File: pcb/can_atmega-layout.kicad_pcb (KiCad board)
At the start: 2 copper layers, 193 x 96 mm, 300 parts, among them J1 Screw_Terminal_01x02, J2 Screw_Terminal_01x02, J3 Conn_01x04_Female, J4 Connector_female, U1 LM1117-5.0, U2 TJA1051T, U3 MCP2515-xSO, U4 ATmega328P-A, X1 16MHz, X2 16MHz

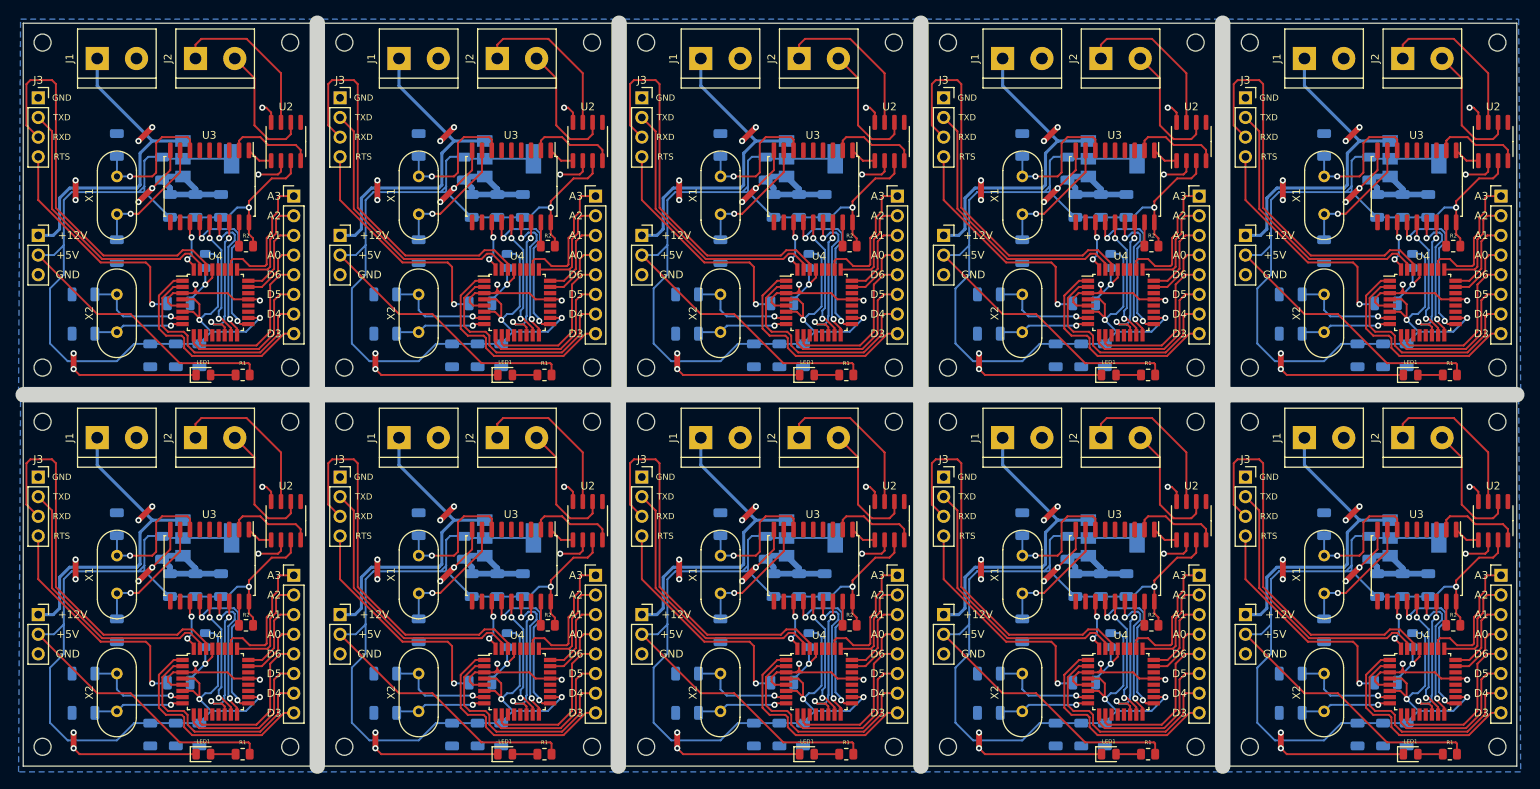
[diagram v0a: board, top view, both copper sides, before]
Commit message: added AVRISP adapter to pcb
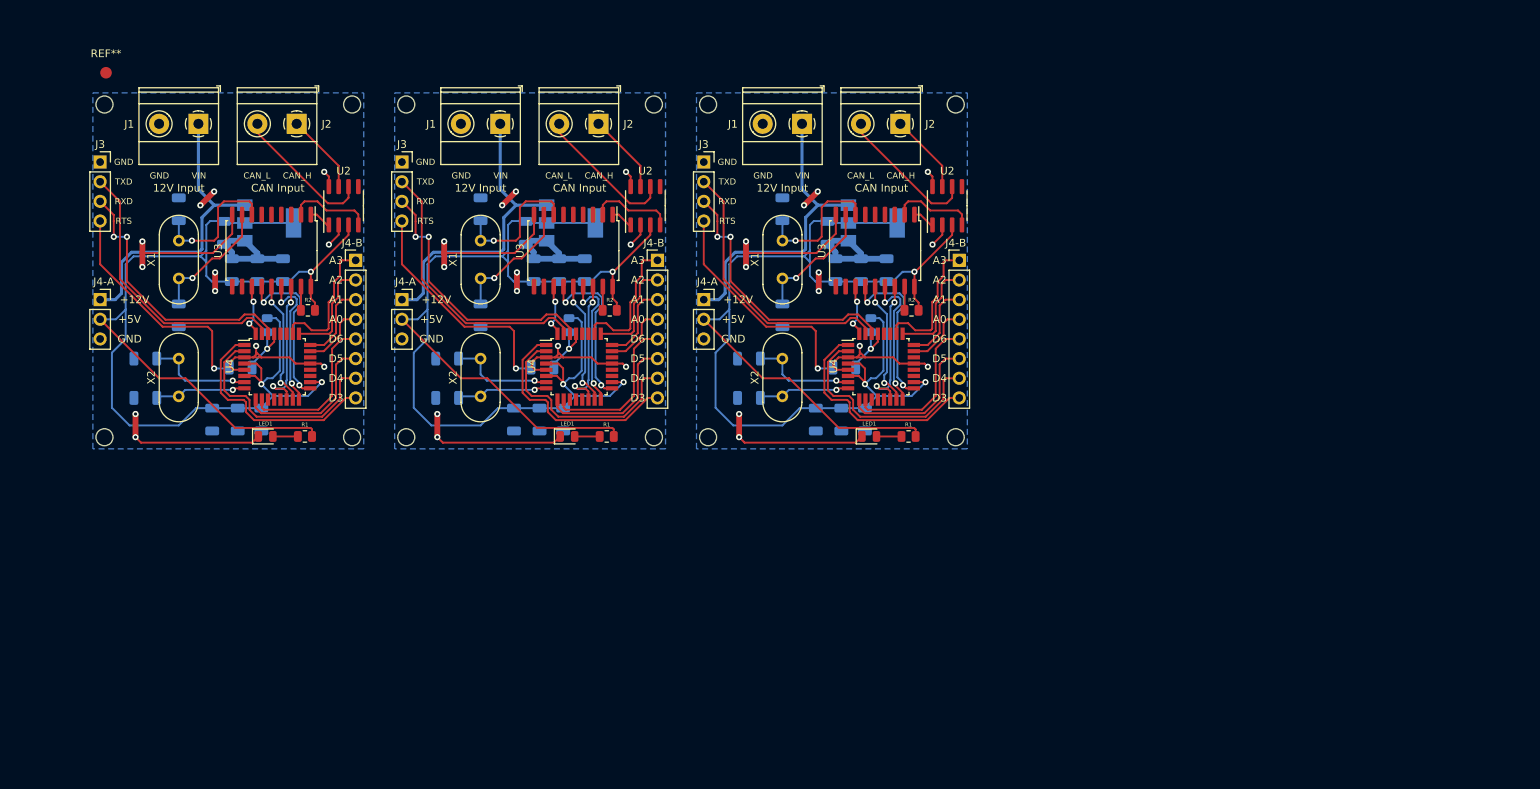
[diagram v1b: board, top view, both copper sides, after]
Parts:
- removed the C1 at (68.9, 79.8)
- removed the C1 at (185.9, 79.8)
- removed the C1 at (29.9, 79.8)
- removed the C1 at (29.9, 30.8)
- removed the C1 at (146.9, 79.8)
- removed the C1 at (185.9, 30.8)
- removed the C1 at (68.9, 30.8)
- removed the C1 at (107.9, 30.8)
- removed the C1 at (107.9, 79.8)
- removed the C1 at (146.9, 30.8)
- removed the C10 at (58.8, 96.0)
- removed the C10 at (136.8, 47.0)
- removed the C10 at (175.8, 96.0)
- removed the C10 at (136.8, 96.0)
- removed the C10 at (19.8, 47.0)
- removed the C10 at (97.8, 96.0)
- removed the C10 at (97.8, 47.0)
- removed the C10 at (175.8, 47.0)
- removed the C10 at (19.8, 96.0)
- removed the C10 at (58.8, 47.0)
- removed the C11 at (19.8, 52.1)
- removed the C11 at (58.8, 101.1)
- removed the C11 at (58.8, 52.1)
- removed the C11 at (97.8, 101.1)
- removed the C11 at (136.8, 101.1)
- removed the C11 at (97.8, 52.1)
- removed the C11 at (19.8, 101.1)
- removed the C11 at (175.8, 52.1)
- removed the C11 at (136.8, 52.1)
- removed the C11 at (175.8, 101.1)
- removed the C12 at (149.1, 97.2)
- removed the C12 at (110.1, 48.2)
- removed the C12 at (188.1, 48.2)
- removed the C12 at (71.1, 48.2)
- removed the C12 at (32.1, 97.2)
- removed the C12 at (32.1, 48.2)
- removed the C12 at (71.1, 97.2)
- removed the C12 at (110.1, 97.2)
- removed the C12 at (149.1, 48.2)
- removed the C12 at (188.1, 97.2)
- removed the C2 at (109.0, 84.6)
- removed the C2 at (148.0, 84.6)
- removed the C2 at (187.0, 84.6)
- removed the C2 at (31.0, 84.6)
- removed the C2 at (70.0, 84.6)
- removed the C2 at (109.0, 35.6)
- removed the C2 at (187.0, 35.6)
- removed the C2 at (70.0, 35.6)
- removed the C2 at (148.0, 35.6)
- removed the C2 at (31.0, 35.6)
- removed the C3 at (34.3, 84.6)
- removed the C3 at (34.3, 35.6)
- removed the C3 at (73.3, 84.6)
- removed the C3 at (73.3, 35.6)
- removed the C3 at (190.3, 35.6)
- removed the C3 at (190.3, 84.6)
- removed the C3 at (112.3, 84.6)
- removed the C3 at (112.3, 35.6)
- removed the C3 at (151.3, 84.6)
- removed the C3 at (151.3, 35.6)
- removed the C4 at (115.6, 35.6)
- removed the C4 at (76.6, 84.6)
- removed the C4 at (193.6, 84.6)
- removed the C4 at (37.6, 84.6)
- removed the C4 at (154.6, 84.6)
- removed the C4 at (37.6, 35.6)
- removed the C4 at (154.6, 35.6)
- removed the C4 at (76.6, 35.6)
- removed the C4 at (193.6, 35.6)
- removed the C4 at (115.6, 84.6)
- removed the C5 at (63.1, 90.5)
- removed the C5 at (63.1, 41.5)
- removed the C5 at (141.1, 90.5)
- removed the C5 at (102.1, 41.5)
- removed the C5 at (24.1, 90.5)
- removed the C5 at (180.1, 41.5)
- removed the C5 at (180.1, 90.5)
- removed the C5 at (141.1, 41.5)
- removed the C5 at (102.1, 90.5)
- removed the C5 at (24.1, 41.5)
- removed the C6 at (180.1, 76.7)
- removed the C6 at (141.1, 76.7)
- removed the C6 at (102.1, 27.7)
- removed the C6 at (63.1, 27.7)
- removed the C6 at (24.1, 27.7)
- removed the C6 at (180.1, 27.7)
- removed the C6 at (63.1, 76.7)
- removed the C6 at (141.1, 27.7)
- removed the C6 at (102.1, 76.7)
- removed the C6 at (24.1, 76.7)
- removed the C7 at (31.7, 54.9)
- removed the C7 at (187.7, 103.9)
- removed the C7 at (187.7, 54.9)
- removed the C7 at (148.7, 54.9)
- removed the C7 at (31.7, 103.9)
- removed the C7 at (70.7, 54.9)
- removed the C7 at (109.7, 54.9)
- removed the C7 at (70.7, 103.9)
- removed the C7 at (148.7, 103.9)
- removed the C7 at (109.7, 103.9)
- removed the C8 at (112.8, 54.9)
- removed the C8 at (73.8, 103.9)
- removed the C8 at (151.8, 54.9)
- removed the C8 at (112.8, 103.9)
- removed the C8 at (34.8, 103.9)
- removed the C8 at (34.8, 54.9)
- removed the C8 at (73.8, 54.9)
- removed the C8 at (190.8, 54.9)
- removed the C8 at (190.8, 103.9)
- removed the C8 at (151.8, 103.9)
- removed the C9 at (145.4, 54.9)
- removed the C9 at (67.4, 103.9)
- removed the C9 at (145.4, 103.9)
- removed the C9 at (184.4, 103.9)
- removed the C9 at (28.4, 54.9)
- removed the C9 at (67.4, 54.9)
- removed the C9 at (28.4, 103.9)
- removed the C9 at (106.4, 103.9)
- removed the C9 at (106.4, 54.9)
- removed the C9 at (184.4, 54.9)
- removed the J1 at (21.6, 16.6)
- removed the J1 at (99.6, 16.6)
- removed the J1 at (60.6, 16.6)
- removed the J1 at (138.6, 16.6)
- removed the J1 at (99.6, 65.6)
- removed the J1 at (21.6, 65.6)
- removed the J1 at (60.6, 65.6)
- removed the J1 at (138.6, 65.6)
- removed the J1 at (177.6, 16.6)
- removed the J1 at (177.6, 65.6)
- removed the J2 at (112.3, 16.6)
- removed the J2 at (151.3, 65.6)
- removed the J2 at (112.3, 65.6)
- removed the J2 at (190.3, 65.6)
- removed the J2 at (151.3, 16.6)
- removed the J2 at (190.3, 16.6)
- removed the J2 at (34.3, 65.6)
- removed the J2 at (73.3, 65.6)
- removed the J2 at (73.3, 16.6)
- removed the J2 at (34.3, 16.6)
- removed the J3 at (13.9, 70.6)
- removed the J3 at (169.9, 70.6)
- removed the J3 at (130.9, 70.6)
- removed the J3 at (169.9, 21.6)
- removed the J3 at (91.9, 21.6)
- removed the J3 at (91.9, 70.6)
- removed the J3 at (52.9, 21.6)
- removed the J3 at (52.9, 70.6)
- removed the J3 at (13.9, 21.6)
- removed the J3 at (130.9, 21.6)
- removed J4 (x10): Connector_female, CAN_ATmega:Connector_female
- removed the LED1 at (113.3, 106.5)
- removed the LED1 at (74.3, 106.5)
- removed the LED1 at (35.3, 57.5)
- removed the LED1 at (152.3, 106.5)
- removed the LED1 at (113.3, 57.5)
- removed the LED1 at (74.3, 57.5)
- removed the LED1 at (152.3, 57.5)
- removed the LED1 at (191.3, 106.5)
- removed the LED1 at (35.3, 106.5)
- removed the LED1 at (191.3, 57.5)
- removed the R1 at (40.4, 57.5)
- removed the R1 at (118.4, 57.5)
- removed the R1 at (157.4, 106.5)
- removed the R1 at (196.4, 106.5)
- removed the R1 at (40.4, 106.5)
- removed the R1 at (196.4, 57.5)
- removed the R1 at (79.4, 106.5)
- removed the R1 at (157.4, 57.5)
- removed the R1 at (118.4, 106.5)
- removed the R1 at (79.4, 57.5)
- removed the R2 at (40.8, 89.8)
- removed the R2 at (157.8, 89.8)
- removed the R2 at (196.8, 89.8)
- removed the R2 at (196.8, 40.8)
- removed the R2 at (157.8, 40.8)
- removed the R2 at (79.8, 40.8)
- removed the R2 at (118.8, 89.8)
- removed the R2 at (79.8, 89.8)
- removed the R2 at (118.8, 40.8)
- removed the R2 at (40.8, 40.8)
- removed the R3 at (152.5, 91.7)
- removed the R3 at (74.5, 91.7)
- removed the R3 at (35.5, 42.7)
- removed the R3 at (113.5, 91.7)
- removed the R3 at (191.5, 91.7)
- removed the R3 at (113.5, 42.7)
- removed the R3 at (74.5, 42.7)
- removed the R3 at (152.5, 42.7)
- removed the R3 at (35.5, 91.7)
- removed the R3 at (191.5, 42.7)
- removed the REF** at (53.5, 14.5)
- removed the REF** at (92.5, 14.5)
- removed the REF** at (14.5, 63.5)
- removed the REF** at (170.5, 56.5)
- removed the REF** at (124.5, 14.5)
- removed the REF** at (85.5, 63.5)
- removed the REF** at (85.5, 14.5)
- removed the REF** at (124.5, 63.5)
- removed the REF** at (53.5, 56.5)
- removed the REF** at (92.5, 63.5)
- removed the REF** at (170.5, 14.5)
- removed the REF** at (14.5, 14.5)
- removed the REF** at (131.5, 14.5)
- removed the REF** at (131.5, 56.5)
- removed the REF** at (14.5, 56.5)
- removed the REF** at (124.5, 105.5)
- removed the REF** at (170.5, 105.5)
- removed the REF** at (14.5, 105.5)
- removed the REF** at (163.5, 63.5)
- removed the REF** at (163.5, 105.5)
- removed the REF** at (53.5, 63.5)
- removed the REF** at (202.5, 14.5)
- removed the REF** at (46.5, 56.5)
- removed the REF** at (53.5, 105.5)
- removed the REF** at (46.5, 14.5)
- removed the REF** at (202.5, 105.5)
- removed the REF** at (131.5, 105.5)
- removed the REF** at (85.5, 56.5)
- removed the REF** at (163.5, 56.5)
- removed the REF** at (124.5, 56.5)
- removed the REF** at (46.5, 105.5)
- removed the REF** at (92.5, 56.5)
- removed the REF** at (163.5, 14.5)
- removed the REF** at (202.5, 56.5)
- removed the REF** at (131.5, 63.5)
- removed the REF** at (85.5, 105.5)
- removed the REF** at (46.5, 63.5)
- removed the REF** at (202.5, 63.5)
- removed the REF** at (170.5, 63.5)
- removed the REF** at (92.5, 105.5)
- removed the U1 at (191.8, 78.5)
- removed the U1 at (152.8, 78.5)
- removed the U1 at (152.8, 29.5)
- removed the U1 at (35.8, 78.5)
- removed the U1 at (35.8, 29.5)
- removed the U1 at (191.8, 29.5)
- removed the U1 at (74.8, 78.5)
- removed the U1 at (113.8, 78.5)
- removed the U1 at (113.8, 29.5)
- removed the U1 at (74.8, 29.5)
- removed the U2 at (84.9, 27.3)
- removed the U2 at (201.9, 27.3)
- removed the U2 at (84.9, 76.3)
- removed the U2 at (45.9, 76.3)
- removed the U2 at (123.9, 76.3)
- removed the U2 at (162.9, 27.3)
- removed the U2 at (201.9, 76.3)
- removed the U2 at (162.9, 76.3)
- removed the U2 at (123.9, 27.3)
- removed the U2 at (45.9, 27.3)
- removed the U3 at (75.1, 33.1)
- removed the U3 at (153.1, 82.1)
- removed the U3 at (192.1, 82.1)
- removed the U3 at (36.1, 82.1)
- removed the U3 at (75.1, 82.1)
- removed the U3 at (153.1, 33.1)
- removed the U3 at (192.1, 33.1)
- removed the U3 at (36.1, 33.1)
- removed the U3 at (114.1, 82.1)
- removed the U3 at (114.1, 33.1)
- removed the U4 at (75.8, 48.1)
- removed the U4 at (153.8, 48.1)
- removed the U4 at (114.8, 48.1)
- removed the U4 at (114.8, 97.1)
- removed the U4 at (36.8, 48.1)
- removed the U4 at (192.8, 48.1)
- removed the U4 at (75.8, 97.1)
- removed the U4 at (36.8, 97.1)
- removed the U4 at (153.8, 97.1)
- removed the U4 at (192.8, 97.1)
- removed the X1 at (63.1, 80.8)
- removed the X1 at (24.1, 80.8)
- removed the X1 at (141.1, 80.8)
- removed the X1 at (180.1, 80.8)
- removed the X1 at (180.1, 31.8)
- removed the X1 at (102.1, 80.8)
- removed the X1 at (141.1, 31.8)
- removed the X1 at (63.1, 31.8)
- removed the X1 at (24.1, 31.8)
- removed the X1 at (102.1, 31.8)
- removed the X2 at (102.1, 96.0)
- removed the X2 at (63.1, 96.0)
- removed the X2 at (102.1, 47.0)
- removed the X2 at (24.1, 96.0)
- removed the X2 at (180.1, 96.0)
- removed the X2 at (63.1, 47.0)
- removed the X2 at (141.1, 96.0)
- removed the X2 at (24.1, 47.0)
- removed the X2 at (180.1, 47.0)
- removed the X2 at (141.1, 47.0)
- added C1: 1uF, Capacitor_SMD:C_1206_3216Metric, B.Cu at (37.9, 39.1)
- added C1: 1uF, Capacitor_SMD:C_1206_3216Metric, B.Cu at (76.9, 39.1)
- added C1: 1uF, Capacitor_SMD:C_1206_3216Metric, B.Cu at (115.9, 39.1)
- added C10: 22PF, Capacitor_SMD:C_1206_3216Metric, B.Cu at (66.8, 55.3)
- added C10: 22PF, Capacitor_SMD:C_1206_3216Metric, B.Cu at (27.8, 55.3)
- added C10: 22PF, Capacitor_SMD:C_1206_3216Metric, B.Cu at (105.8, 55.3)
- added C11: 22PF, Capacitor_SMD:C_1206_3216Metric, B.Cu at (105.8, 60.4)
- added C11: 22PF, Capacitor_SMD:C_1206_3216Metric, B.Cu at (27.8, 60.4)
- added C11: 22PF, Capacitor_SMD:C_1206_3216Metric, B.Cu at (66.8, 60.4)
- added C12: 1uF, Capacitor_SMD:C_1206_3216Metric, B.Cu at (79.1, 56.5)
- added C12: 1uF, Capacitor_SMD:C_1206_3216Metric, B.Cu at (118.1, 56.5)
- added C12: 1uF, Capacitor_SMD:C_1206_3216Metric, B.Cu at (40.1, 56.5)
- added C2: 10uF/16V, Capacitor_SMD:C_1206_3216Metric, B.Cu at (117.0, 43.9)
- added C2: 10uF/16V, Capacitor_SMD:C_1206_3216Metric, B.Cu at (39.0, 43.9)
- added C2: 10uF/16V, Capacitor_SMD:C_1206_3216Metric, B.Cu at (78.0, 43.9)
- added C3: 0.1uF, Capacitor_SMD:C_1206_3216Metric, B.Cu at (81.3, 43.9)
- added C3: 0.1uF, Capacitor_SMD:C_1206_3216Metric, B.Cu at (42.3, 43.9)
- added C3: 0.1uF, Capacitor_SMD:C_1206_3216Metric, B.Cu at (120.3, 43.9)
- added C4: 0.1uF, Capacitor_SMD:C_1206_3216Metric, B.Cu at (123.6, 43.9)
- added C4: 0.1uF, Capacitor_SMD:C_1206_3216Metric, B.Cu at (45.6, 43.9)
- added C4: 0.1uF, Capacitor_SMD:C_1206_3216Metric, B.Cu at (84.6, 43.9)
- added C5: 22PF, Capacitor_SMD:C_1206_3216Metric, B.Cu at (71.1, 49.8)
- added C5: 22PF, Capacitor_SMD:C_1206_3216Metric, B.Cu at (32.1, 49.8)
- added C5: 22PF, Capacitor_SMD:C_1206_3216Metric, B.Cu at (110.1, 49.8)
- added C6: 22PF, Capacitor_SMD:C_1206_3216Metric, B.Cu at (110.1, 36.0)
- added C6: 22PF, Capacitor_SMD:C_1206_3216Metric, B.Cu at (71.1, 36.0)
- added C6: 22PF, Capacitor_SMD:C_1206_3216Metric, B.Cu at (32.1, 36.0)
- added C7: 0.1uF, Capacitor_SMD:C_1206_3216Metric, B.Cu at (78.7, 63.2)
- added C7: 0.1uF, Capacitor_SMD:C_1206_3216Metric, B.Cu at (39.7, 63.2)
- added C7: 0.1uF, Capacitor_SMD:C_1206_3216Metric, B.Cu at (117.7, 63.2)
- added C8: 10uF/16V, Capacitor_SMD:C_1206_3216Metric, B.Cu at (120.8, 63.2)
- added C8: 10uF/16V, Capacitor_SMD:C_1206_3216Metric, B.Cu at (42.8, 63.2)
- added C8: 10uF/16V, Capacitor_SMD:C_1206_3216Metric, B.Cu at (81.8, 63.2)
- added C9: 0.1uF, Capacitor_SMD:C_1206_3216Metric, B.Cu at (114.4, 63.2)
- added C9: 0.1uF, Capacitor_SMD:C_1206_3216Metric, B.Cu at (75.4, 63.2)
- added C9: 0.1uF, Capacitor_SMD:C_1206_3216Metric, B.Cu at (36.4, 63.2)
- added J1: Screw_Terminal_01x02, TerminalBlock_Phoenix:TerminalBlock_Phoenix_MKDS-1,5-2-5.08_1x02_P5.08mm_Horizontal, F.Cu at (73.6, 25.0)
- added J1: Screw_Terminal_01x02, TerminalBlock_Phoenix:TerminalBlock_Phoenix_MKDS-1,5-2-5.08_1x02_P5.08mm_Horizontal, F.Cu at (34.6, 25.0)
- added J1: Screw_Terminal_01x02, TerminalBlock_Phoenix:TerminalBlock_Phoenix_MKDS-1,5-2-5.08_1x02_P5.08mm_Horizontal, F.Cu at (112.6, 25.0)
- added J2: Screw_Terminal_01x02, TerminalBlock_Phoenix:TerminalBlock_Phoenix_MKDS-1,5-2-5.08_1x02_P5.08mm_Horizontal, F.Cu at (86.3, 25.0)
- added J2: Screw_Terminal_01x02, TerminalBlock_Phoenix:TerminalBlock_Phoenix_MKDS-1,5-2-5.08_1x02_P5.08mm_Horizontal, F.Cu at (125.3, 25.0)
- added J2: Screw_Terminal_01x02, TerminalBlock_Phoenix:TerminalBlock_Phoenix_MKDS-1,5-2-5.08_1x02_P5.08mm_Horizontal, F.Cu at (47.3, 25.0)
- added J3: Conn_01x04_Female, Connector_PinSocket_2.54mm:PinSocket_1x04_P2.54mm_Vertical, F.Cu at (60.9, 29.9)
- added J3: Conn_01x04_Female, Connector_PinSocket_2.54mm:PinSocket_1x04_P2.54mm_Vertical, F.Cu at (99.9, 29.9)
- added J3: Conn_01x04_Female, Connector_PinSocket_2.54mm:PinSocket_1x04_P2.54mm_Vertical, F.Cu at (21.9, 29.9)
- added J4-A: Connector_female, CAN_ATmega:Connector_female, F.Cu at (37.2, 50.3)
- added J4-A: Connector_female, CAN_ATmega:Connector_female, F.Cu at (115.2, 50.3)
- added J4-A: Connector_female, CAN_ATmega:Connector_female, F.Cu at (76.2, 50.3)
- added LED1: Green, LED_SMD:LED_0805_2012Metric, F.Cu at (82.3, 65.4)
- added LED1: Green, LED_SMD:LED_0805_2012Metric, F.Cu at (121.3, 65.4)
- added LED1: Green, LED_SMD:LED_0805_2012Metric, F.Cu at (43.3, 65.4)
- added R1: 1K, Resistor_SMD:R_0805_2012Metric, F.Cu at (48.4, 65.4)
- added R1: 1K, Resistor_SMD:R_0805_2012Metric, F.Cu at (87.4, 65.4)
- added R1: 1K, Resistor_SMD:R_0805_2012Metric, F.Cu at (126.4, 65.4)
- added R2: 10K, Resistor_SMD:R_0805_2012Metric, F.Cu at (48.8, 49.1)
- added R2: 10K, Resistor_SMD:R_0805_2012Metric, F.Cu at (126.8, 49.1)
- added R2: 10K, Resistor_SMD:R_0805_2012Metric, F.Cu at (87.8, 49.1)
- added R3: 10K, Resistor_SMD:R_0805_2012Metric, B.Cu at (43.5, 51.0)
- added R3: 10K, Resistor_SMD:R_0805_2012Metric, B.Cu at (82.5, 51.0)
- added R3: 10K, Resistor_SMD:R_0805_2012Metric, B.Cu at (121.5, 51.0)
- added REF**: MountingHole_2.2mm_M2, MountingHole:MountingHole_2.2mm_M2, F.Cu at (61.5, 22.5)
- added REF**: MountingHole_2.2mm_M2, MountingHole:MountingHole_2.2mm_M2, F.Cu at (22.5, 65.5)
- added REF**: MountingHole_2.2mm_M2, MountingHole:MountingHole_2.2mm_M2, F.Cu at (54.5, 65.5)
- added REF**: MountingHole_2.2mm_M2, MountingHole:MountingHole_2.2mm_M2, F.Cu at (100.5, 22.5)
- added REF**: MountingHole_2.2mm_M2, MountingHole:MountingHole_2.2mm_M2, F.Cu at (54.5, 22.5)
- added REF**: MountingHole_2.2mm_M2, MountingHole:MountingHole_2.2mm_M2, F.Cu at (93.5, 22.5)
- added REF**: MountingHole_2.2mm_M2, MountingHole:MountingHole_2.2mm_M2, F.Cu at (22.5, 22.5)
- added REF**: MountingHole_2.2mm_M2, MountingHole:MountingHole_2.2mm_M2, F.Cu at (93.5, 65.5)
- added REF**: MountingHole_2.2mm_M2, MountingHole:MountingHole_2.2mm_M2, F.Cu at (132.5, 65.5)
- added REF**: Fiducial_1.5mm_Mask3mm, Fiducial:Fiducial_1.5mm_Mask3mm, F.Cu at (22.7, 18.4)
- added REF**: MountingHole_2.2mm_M2, MountingHole:MountingHole_2.2mm_M2, F.Cu at (132.5, 22.5)
- added REF**: MountingHole_2.2mm_M2, MountingHole:MountingHole_2.2mm_M2, F.Cu at (100.5, 65.5)
- added REF**: MountingHole_2.2mm_M2, MountingHole:MountingHole_2.2mm_M2, F.Cu at (61.5, 65.5)
- added U1: LM1117-5.0, Package_TO_SOT_SMD:SOT-223, B.Cu at (82.8, 37.8)
- added U1: LM1117-5.0, Package_TO_SOT_SMD:SOT-223, B.Cu at (43.8, 37.8)
- added U1: LM1117-5.0, Package_TO_SOT_SMD:SOT-223, B.Cu at (121.8, 37.8)
- added U2: TJA1051T, Package_SO:SOIC-8_3.9x4.9mm_P1.27mm, F.Cu at (53.4, 35.6)
- added U2: TJA1051T, Package_SO:SOIC-8_3.9x4.9mm_P1.27mm, F.Cu at (92.4, 35.6)
- added U2: TJA1051T, Package_SO:SOIC-8_3.9x4.9mm_P1.27mm, F.Cu at (131.4, 35.6)
- added U3: MCP2515-xSO, Package_SO:SOIC-18W_7.5x11.6mm_P1.27mm, F.Cu at (83.1, 41.4)
- added U3: MCP2515-xSO, Package_SO:SOIC-18W_7.5x11.6mm_P1.27mm, F.Cu at (122.1, 41.4)
- added U3: MCP2515-xSO, Package_SO:SOIC-18W_7.5x11.6mm_P1.27mm, F.Cu at (44.1, 41.4)
- added U4: ATmega328P-A, Package_QFP:TQFP-32_7x7mm_P0.8mm, F.Cu at (83.8, 56.4)
- added U4: ATmega328P-A, Package_QFP:TQFP-32_7x7mm_P0.8mm, F.Cu at (44.8, 56.4)
- added U4: ATmega328P-A, Package_QFP:TQFP-32_7x7mm_P0.8mm, F.Cu at (122.8, 56.4)
- added X1: 16MHz, Crystal:Crystal_HC49-4H_Vertical, F.Cu at (110.1, 40.1)
- added X1: 16MHz, Crystal:Crystal_HC49-4H_Vertical, F.Cu at (32.1, 40.1)
- added X1: 16MHz, Crystal:Crystal_HC49-4H_Vertical, F.Cu at (71.1, 40.1)
- added X2: 16MHz, Crystal:Crystal_HC49-4H_Vertical, F.Cu at (71.1, 55.3)
- added X2: 16MHz, Crystal:Crystal_HC49-4H_Vertical, F.Cu at (32.1, 55.3)
- added X2: 16MHz, Crystal:Crystal_HC49-4H_Vertical, F.Cu at (110.1, 55.3)
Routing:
- net +5V: track 1677.2 -> 503.7 mm, vias 30 -> 9
- net GND: track 704.0 -> 242.8 mm, vias 120 -> 36
- net U4_RXD: track 514.4 -> 104.4 mm, vias 0 -> 6
- net +12V: track 421.0 -> 119.6 mm
- net U4_TXD: track 359.4 -> 107.8 mm
- net U4_RTS: track 305.7 -> 91.7 mm, vias 10 -> 3
- net U4_D4: track 294.3 -> 88.3 mm
- net U4_D3: track 289.4 -> 86.8 mm
- net /CAN_H: track 213.3 -> 31.1 mm
- net SCK: track 212.3 -> 63.7 mm, vias 20 -> 6
- net U4_D6: track 206.4 -> 61.9 mm
- net U4_D5: track 197.2 -> 59.2 mm
- net SO: track 182.8 -> 54.8 mm, vias 20 -> 6
- net CS: track 181.1 -> 54.3 mm, vias 20 -> 6
- net /U3_OSC_2: track 179.0 -> 53.7 mm, vias 10 -> 3
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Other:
- board outline removed
- board text added: "12V Input"
- board text added: "CAN Input"
- board text added: "CAN_H"
- board text added: "CAN_L"
- board text added: "J4-B"
- board text added: "VIN"
